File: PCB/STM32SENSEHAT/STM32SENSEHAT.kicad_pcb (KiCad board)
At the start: 2 copper layers, 100 x 100 mm, 82 parts, among them J1 USB_B_Micro, J10 Conn_01x01_Pin, J11 Conn_01x02_Pin, J2 Conn_01x05_Pin, J5 Conn_01x24_Pin, J8 Conn_01x24_Pin, J9 Conn_01x10_Pin, Q1 FS8205A, SW1 SW_Push, U1 MCP1700x-330xxTT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

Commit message: Final draft pending review
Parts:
- removed the C19 at (121.4, 95.9)
- removed the D1 at (131.5, 101.7)
- added G***: LOGO, logos:gitlab2, F.Cu at (153.1, 134.6)
- added G***: LOGO, logos:UCT4, F.Cu at (169.6, 134.5)
- added G***: LOGO, logos:BARCA, B.Cu at (151.2, 94.4)
- moved C18 8.81 mm to (132.9, 71.3), turned to 90 degrees
- moved C10 8.79 mm to (122.0, 95.6), turned to 180 degrees
- moved R4 5.33 mm to (113.6, 96.3)
- moved JP2 3.47 mm to (190.5, 104.7)
- moved C17 3.44 mm to (128.6, 71.2), turned to 90 degrees
- moved TP5 3.42 mm to (105.7, 78.7)
- moved J10 3.35 mm to (195.2, 104.7)
- moved R7 3.02 mm to (106.2, 98.7)
- moved R2 2.77 mm to (118.2, 123.4)
- moved R3 2.77 mm to (118.3, 126.7)
- moved U3 2.77 mm to (118.7, 130.3)
- moved C11 2.64 mm to (115.5, 84.0)
- moved D2 2.46 mm to (105.1, 92.5)
- moved J2 2.39 mm to (121.1, 119.2)
- moved U1 2.21 mm to (109.9, 86.0)
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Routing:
- net 5VUSB: track 183.3 -> 248.6 mm, vias 0 -> 3
- net Net-(U4-V+): track 5.18 -> 45.0 mm
- net /MCU MODULE/USB_DN: track 120.5 -> 157.2 mm, vias 4 -> 2
- net 3V3: track 264.3 -> 297.2 mm
- net /MCU MODULE/PB6: track 82.6 -> 112.8 mm
- net /MCU MODULE/PA5: track 102.0 -> 130.3 mm, vias 1 -> 0
- net GND: track 54.4 -> 31.2 mm, vias 2 -> 14
- net /MCU MODULE/USB_DP: track 111.4 -> 127.0 mm
- net /POWER MANAGEMENT MODULE/BATT+: track 54.9 -> 70.0 mm, vias 4 -> 0
- net Net-(D4-K): track 17.3 -> 31.9 mm, vias 1 -> 0
- net Net-(BT2--): track 117.1 -> 131.2 mm
- net /MCU MODULE/NRST: track 112.1 -> 125.2 mm
- net Net-(D5-K): track 8.23 -> 20.9 mm, vias 1 -> 0
- net /MCU MODULE/PA14: track 67.3 -> 79.6 mm
- net Net-(U2-VDD): track 14.2 -> 26.2 mm, vias 2 -> 0
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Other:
- board text added: "3V3"
- board text added: "5V"
- board text added: "BACK-UP SENSOR"
- board text added: "BOOT"
- board text added: "CHARGE"
- board text added: "D_N"
- board text added: "D_P"
- board text added: "EEPROM"
- board text added: "FOR SET UP INSTRUCTIONS SCAN QR CODE"
- board text added: "GND"
- board text added: "GPIO"
- board text added: "GROUP 7 Name Student # Rumbidzai Mashumba MSHRUM006 Phomolo Makina MKNPH0002 Travimadox Webb WBBTRA001"
- board text added: "NC"
- board text added: "NRST"
- board text added: "PA0"
- board text added: "PA1"
- board text added: "PA10"
- board text added: "PA11"
- board text added: "PA12"
- board text added: "PA13"
- board text added: "PA14"
- board text added: "PA15"
- board text added: "PA2"
- board text added: "PA3"
- board text added: "PA4"
- board text added: "PA5"
- board text added: "PA6"
- board text added: "PA7"
- board text added: "PA8"
- board text added: "PA9"
- board text added: "PB0"
- board text added: "PB1"
- board text added: "PB10"
- board text added: "PB11"
- board text added: "PB12"
- board text added: "PB13"
- board text added: "PB14"
- board text added: "PB15"
- board text added: "PB2"
- board text added: "PB3"
- board text added: "PB4"
- board text added: "PB5"
- board text added: "PB6"
- board text added: "PB7"
- board text added: "PB8"
- board text added: "PB9"
- board text added: "PC13"
- board text added: "PC14"
- board text added: "PC15"
- board text added: "PF0"
- board text added: "PF1"
- board text added: "PF6"
- board text added: "PF7"
- board text added: "POWER-MODULE ↑"
- board text added: "PWR-ON"
- board text added: "Prototype V0.0"
- board text added: "RESET"
- board text added: "SCL-LTR"
- board text added: "SCL-TMP"
- board text added: "SDA-LTR"
- board text added: "SDA_TMP"
- board text added: "SENSOR-DATA-DEBUG"
- board text added: "STAND-BY"
- board text added: "USB-COMMS ↓"
- board text added: "USB-DEBUG"
- board text added: "VBAT"
- board text added: "VBUS"
- board text added: "VDD"
- board text added: "VDDA"
- board text added: "VSS"
- board text added: "VSSA"
- board text added: "©IMPERIUM"

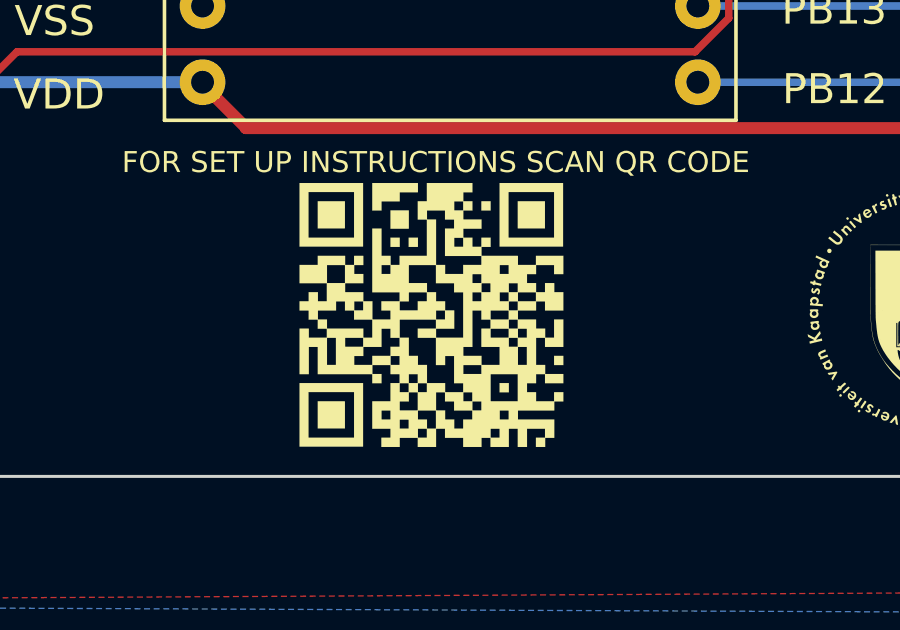
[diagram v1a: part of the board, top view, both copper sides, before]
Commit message: Changed the QR Code on PCB
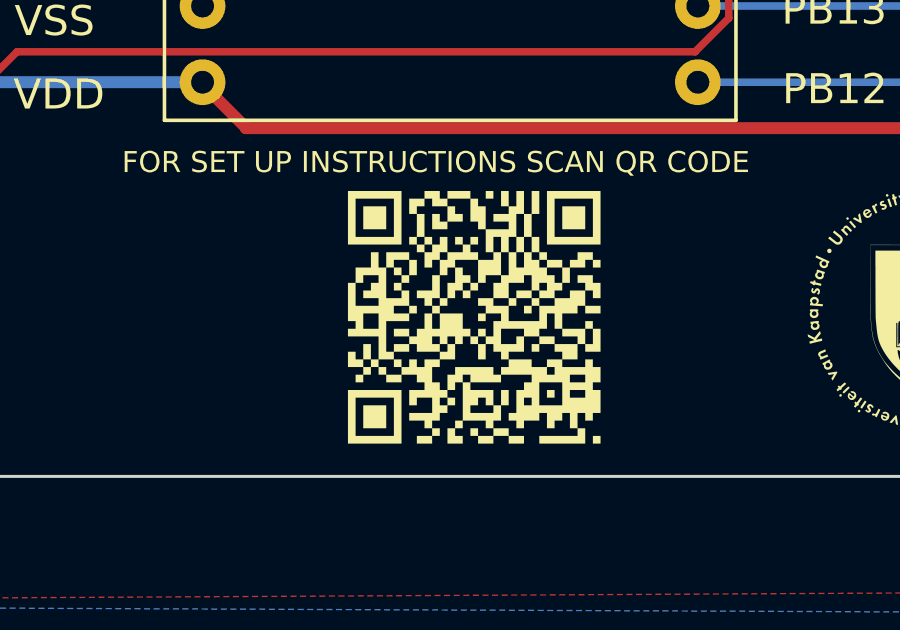
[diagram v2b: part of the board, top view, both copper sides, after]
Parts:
- removed the G*** at (153.1, 134.6)
- added G***: LOGO, logos:qrcodeadobe, F.Cu at (154.6, 134.7)
